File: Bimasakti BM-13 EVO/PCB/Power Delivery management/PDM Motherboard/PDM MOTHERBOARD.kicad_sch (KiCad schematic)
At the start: 25 parts

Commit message: ketinggalan hehe
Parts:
- added N1: pdm 3.3V, Symbol:OSHW-Symbol_6.7x6mm_SilkScreen, symbol Mechanical:Housing
- added N2: pdm 5v, Symbol:OSHW-Symbol_6.7x6mm_SilkScreen, symbol Mechanical:Housing
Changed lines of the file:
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@@
+	)
+	(symbol
+		(lib_id "Mechanical:Housing")
+		(at 74.93 133.35 0)
+		(unit 1)
+		(exclude_from_sim no)
+		(in_bom yes)
+		(on_board yes)
+		(dnp no)
+		(fields_autoplaced yes)
+		(property "Reference" "N1"
+			(at 78.74 132.3974 0)
+			(effects
+				(font
+					(size 1.27 1.27)
+				)
+				(justify left)
+			)
+		)
+		(property "Value" "pdm 3.3V"
+			(at 78.74 134.9374 0)
+			(effects
+				(font
+					(size 1.27 1.27)
+				)
+				(justify left)
+			)
+		)
+		(property "Footprint" "Symbol:OSHW-Symbol_6.7x6mm_SilkScreen"
+			(at 76.2 132.08 0)
+			(effects
+				(font
+					(size 1.27 1.27)
+				)
+				(hide yes)
+			)
+		)
+		(property "Datasheet" "~"
+			(at 76.2 132.08 0)
+			(effects
+				(font
+					(size 1.27 1.27)
+				)
+				(hide yes)
+			)
+		)
+		(property "Description" "Housing"
+			(at 74.93 133.35 0)
+			(effects
+				(font
+					(size 1.27 1.27)
+				)
+				(hide yes)
+			)
+		)
+		(instances
+			(project ""
+				(path "/82d2afdc-f667-482e-a251-d2e6670c33b7"
+					(reference "N1")
+					(unit 1)
+				)
+			)
+		)
 	)
 	(symbol
@@
 					(unit 1)
 				)
+			)
+		)
+	)
+	(symbol
+		(lib_id "Mechanical:Housing")
+		(at 96.52 134.62 0)
+		(unit 1)
+		(exclude_from_sim no)
+		(in_bom yes)
+		(on_board yes)
+		(dnp no)
+		(fields_autoplaced yes)
+		(property "Reference" "N2"
+			(at 100.33 133.6674 0)
+			(effects
+				(font
+					(size 1.27 1.27)
+				)
+				(justify left)
+			)
+		)
+		(property "Value" "pdm 5v"
+			(at 100.33 136.2074 0)
+			(effects
+				(font
+					(size 1.27 1.27)
+				)
+				(justify left)
+			)
+		)
+		(property "Footprint" "Symbol:OSHW-Symbol_6.7x6mm_SilkScreen"
+			(at 97.79 133.35 0)
+			(effects
+				(font
+					(size 1.27 1.27)
+				)
+				(hide yes)
+			)
+		)
+		(property "Datasheet" "~"
+			(at 97.79 133.35 0)
+			(effects
+				(font
+					(size 1.27 1.27)
+				)
+				(hide yes)
+			)
+		)
+		(property "Description" "Housing"
+			(at 96.52 134.62 0)
+			(effects
+				(font
+					(size 1.27 1.27)
+				)
+				(hide yes)
+			)
+		)
+		(instances
+			(project "PDM MOTHERBOARD"
+				(path "/82d2afdc-f667-482e-a251-d2e6670c33b7"
+					(reference "N2")
+					(unit 1)
+				)

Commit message: cicil assembly
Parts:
- added H1, H2, H3, H4: MountingHole_Pad, MountingHole:MountingHole_3.2mm_M3_ISO7380_Pad_TopBottom, symbol Mechanical:MountingHole_Pad
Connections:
- net GND: now also 12in1.1 (Pin_1), D1.2 (A2), F1.1, H1.1, H2.1, H3.1, H4.1

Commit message: ngecilin pdm
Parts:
- removed 12out1, 12out2, 3Vin1, 5Vin1: ~, Connector_JST:JST_EH_B2B-EH-A_1x02_P2.50mm_Vertical, symbol Connector:Conn_01x02_Socket
- removed F1, F10, F3, F4, F5, F6, F7, F8: 1A, Fuse:Fuseholder_Cylinder-5x20mm_Schurter_0031_8201_Horizontal_Open, symbol Device:Fuse
- removed N1: pdm 3.3V, Symbol:OSHW-Symbol_6.7x6mm_SilkScreen, symbol Mechanical:Housing
- removed N2: pdm 5v, Symbol:OSHW-Symbol_6.7x6mm_SilkScreen, symbol Mechanical:Housing
- added F2, F3, F4, F5, F6, F7, F8, F9: 3557-2, 0_FUSE:0_FUSE_3557-2, symbol 0_fuse_3557-2:3557-2
- added U2: ~, BIMS_BUCK:BIMS_BUCK, symbol 0_BUCK:BIMS_BUCK_3V3
- added U3: ~, BIMS_BUCK:BIMS_BUCK, symbol 0_BUCK:BIMS_BUCK_5V
- 12in1: footprint Connector_JST:JST_EH_B2B-EH-A_1x02_P2.50mm_Vertical -> TerminalBlock_TE-Connectivity:TerminalBlock_TE_282834-2_1x02_P2.54mm_Horizontal
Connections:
- net +12: now also F7.1_1, F7.1_2, U2.10 (12VIN), U2.6 (12VIN), U2.7 (12VIN), U2.8 (12VIN), U2.9 (12VIN), U3.10 (12VIN), U3.6 (12VIN), U3.7 (12VIN), U3.8 (12VIN), U3.9 (12VIN)
- net 3Vin: now also F2.1_1, F2.1_2, F3.1_1, F3.1_2, U2.16 (3V3), U2.17 (3V3), U2.18 (3V3), U2.19 (3V3), U2.20 (3V3)
- net 5Vin: now also F4.1_1, F4.1_2, F5.1_1, F5.1_2, F6.1_1, F6.1_2, F8.1_1, F8.1_2, U3.16 (5V), U3.17 (5V), U3.18 (5V), U3.19 (5V), U3.20 (5V)
- net GND: now also U2.1 (GND), U2.11 (GND), U2.12 (GND), U2.13 (GND), U2.14 (GND), U2.15 (GND), U2.2 (GND), U2.3 (GND), U2.4 (GND), U2.5 (GND), U3.1 (GND), U3.11 (GND), U3.12 (GND), U3.13 (GND), U3.14 (GND), U3.15 (GND), U3.2 (GND), U3.3 (GND), U3.4 (GND), U3.5 (GND)
- net at 3v3out2.1 (Pin_1): now also F3.2_1, F3.2_2
- net at 12in1.2 (Pin_2), D1.1 (A1): now also F9.1_1, F9.1_2; no longer U1.1 (D)
- net at 12vout1.1 (Pin_1): now also F7.2_1, F7.2_2
- net at 5out3.1 (Pin_1): now also F6.2_1, F6.2_2
- net at 5out2.1 (Pin_1): now also F8.2_1, F8.2_2
- net at 5out1.1 (Pin_1): now also F4.2_1, F4.2_2
- net at 5out4.1 (Pin_1): now also F5.2_1, F5.2_2
- net at 3v3out1.1 (Pin_1): now also F2.2_1, F2.2_2
- new net: F9.2_1, F9.2_2, U1.1 (D)
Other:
- moved on the sheet: 12in1, 12vout1, 3v3out1, 3v3out2, 5out1, 5out3, 5out4, D1, D5

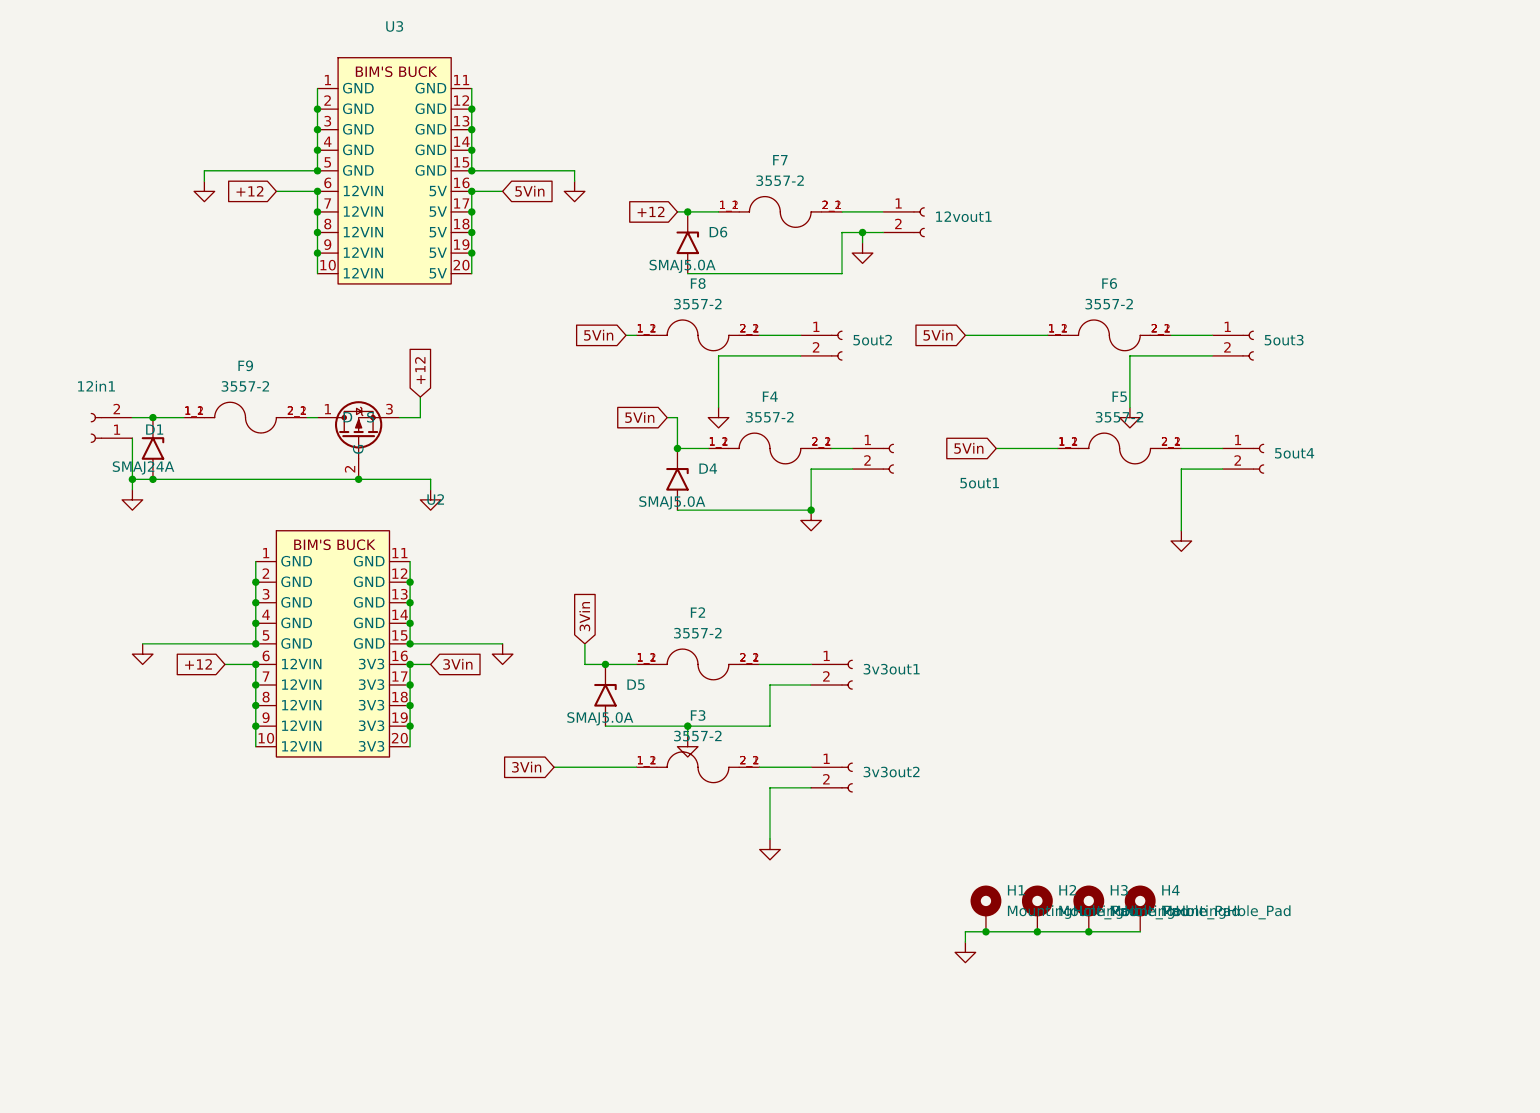
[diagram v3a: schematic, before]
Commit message: pdm selesai ril, tv board sudah bagus kurang cek (mungkin ganti konektor)
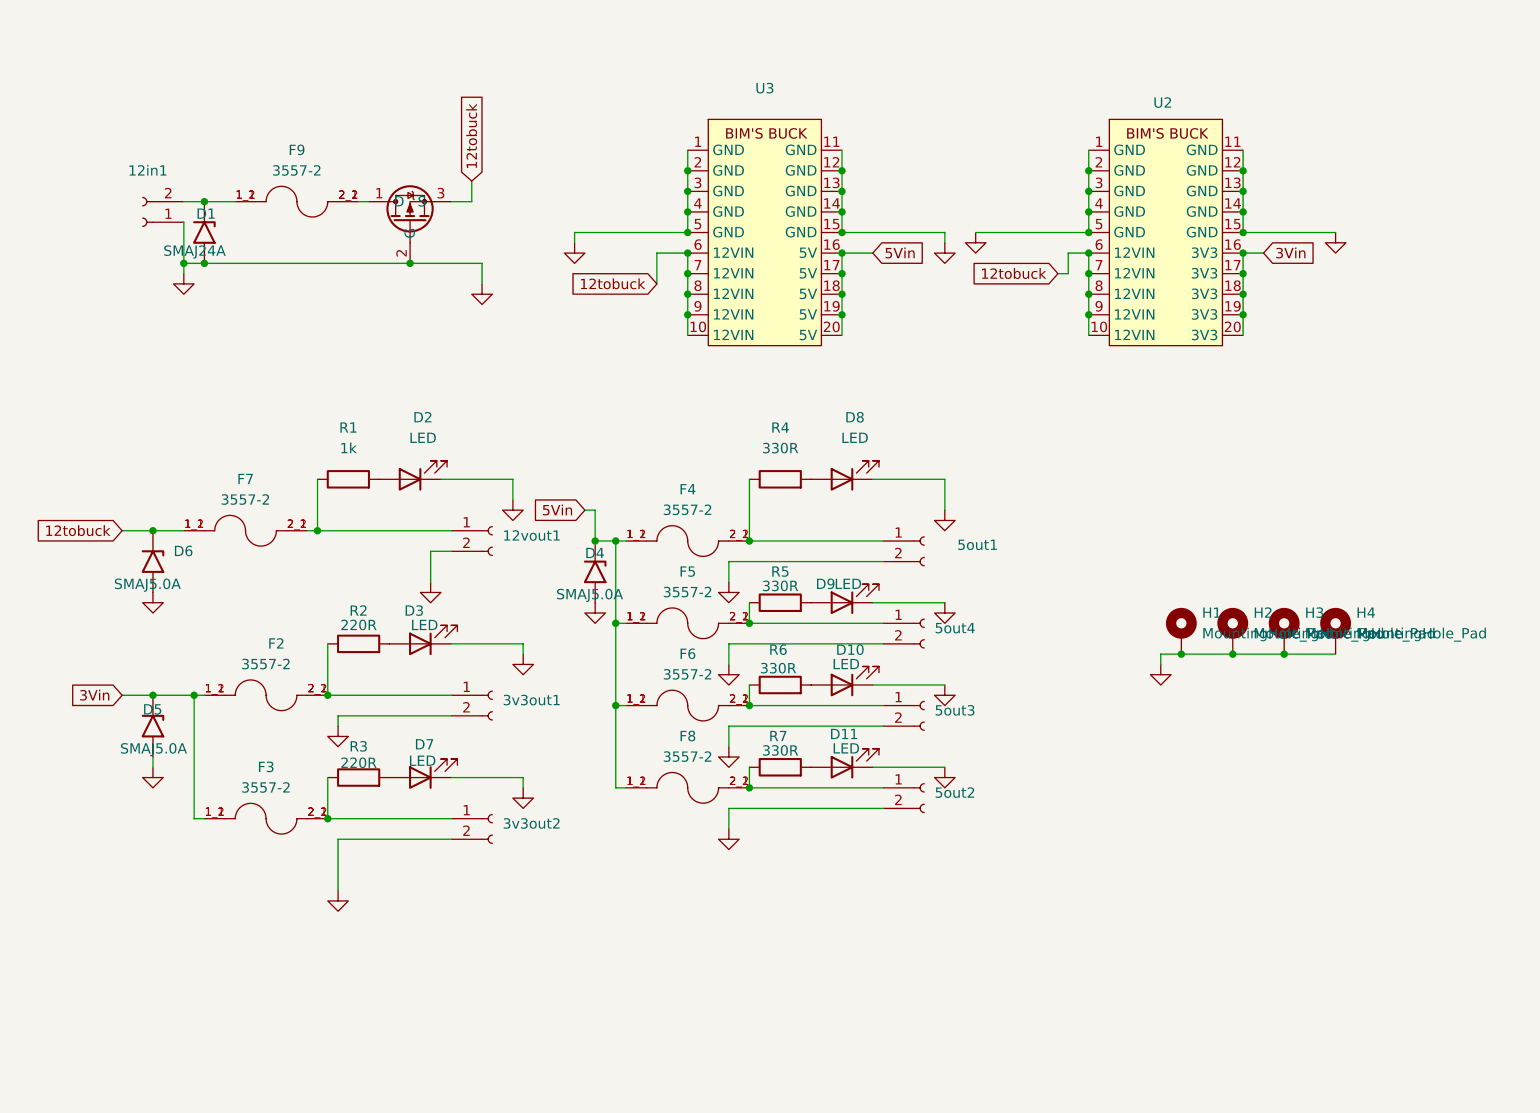
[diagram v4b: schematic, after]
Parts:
- added D10, D11, D2, D3, D7, D8, D9: LED, LED_SMD:LED_0805_2012Metric_Pad1.15x1.40mm_HandSolder, symbol Device:LED
- added R1: 1k, Resistor_SMD:R_0805_2012Metric_Pad1.20x1.40mm_HandSolder, symbol Device:R
- added R2, R3: 220R, Resistor_SMD:R_0805_2012Metric_Pad1.20x1.40mm_HandSolder, symbol Device:R
- added R4, R5, R6, R7: 330R, Resistor_SMD:R_0805_2012Metric_Pad1.20x1.40mm_HandSolder, symbol Device:R
- 12in1: footprint TerminalBlock_TE-Connectivity:TerminalBlock_TE_282834-2_1x02_P2.54mm_Horizontal -> TerminalBlock_Phoenix:TerminalBlock_Phoenix_MKDS-1,5-2_1x02_P5.00mm_Horizontal
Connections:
- net GND: now also D10.1 (K), D11.1 (K), D2.1 (K), D3.1 (K), D7.1 (K), D8.1 (K), D9.1 (K)
- net at 3v3out2.1 (Pin_1), F3.2_1, F3.2_2: now also R3.1
- net at 5out4.1 (Pin_1), F5.2_1, F5.2_2: now also R5.1
- net at 5out3.1 (Pin_1), F6.2_1, F6.2_2: now also R6.1
- net at 5out2.1 (Pin_1), F8.2_1, F8.2_2: now also R7.1
- net at 5out1.1 (Pin_1), F4.2_1, F4.2_2: now also R4.1
- net at 12vout1.1 (Pin_1), F7.2_1, F7.2_2: now also R1.1
- net at 3v3out1.1 (Pin_1), F2.2_1, F2.2_2: now also R2.1
- net +12 renamed 12tobuck
- new net: D2.2 (A), R1.2
- new net: D7.2 (A), R3.2
- new net: D9.2 (A), R5.2
- new net: D10.2 (A), R6.2
- new net: D11.2 (A), R7.2
- new net: D8.2 (A), R4.2
- new net: D3.2 (A), R2.2
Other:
- moved on the sheet: 12in1, 12vout1, 3v3out1, 3v3out2, 5out1, 5out2, 5out3, 5out4, D1, D4, D5, D6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

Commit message: buat placeholder baru dan ganti konektor
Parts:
- 5out2: footprint Connector_JST:JST_EH_B2B-EH-A_1x02_P2.50mm_Vertical -> Connector_Molex:Molex_Nano-Fit_105309-xx02_1x02_P2.50mm_Vertical
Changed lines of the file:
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@@
 			)
 		)
-		(property "Footprint" "Connector_JST:JST_EH_B2B-EH-A_1x02_P2.50mm_Vertical"
+		(property "Footprint" "Connector_Molex:Molex_Nano-Fit_105309-xx02_1x02_P2.50mm_Vertical"
 			(at 121.92 119.38 0)
 			(effects

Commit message: update
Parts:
- added D12: LED, LED_SMD:LED_0805_2012Metric_Pad1.15x1.40mm_HandSolder, symbol Device:LED
- added R8: 1k, Resistor_SMD:R_0805_2012Metric_Pad1.20x1.40mm_HandSolder, symbol Device:R
- renumbered 3v3out2 to 5out5
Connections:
- net 3Vin: no longer F3.1_1, F3.1_2
- net 5Vin: now also F3.1_1, F3.1_2
- net GND: now also D12.1 (K)
- net at 12in1.2 (Pin_2), D1.1 (A1), F9.1_1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: now also R8.1
- new net: D12.2 (A), R8.2
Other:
- note added: "12V Output"
- note added: "3V3 Output"
- note added: "5V Output"
- moved on the sheet: 12vout1, 3v3out1, 5out1, 5out2, 5out3, 5out4, 5out5, D10, D11, D2, D3, D4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
